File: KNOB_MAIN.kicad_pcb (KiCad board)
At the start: 2 copper layers, 100 x 30 mm, 21 parts, among them J1 HRO_TYPE-C-31-M-12, SW1 PEC11R-4220F-S0024, U1 AMS1117-3.3, U2 ESP32-C3-MINI-1

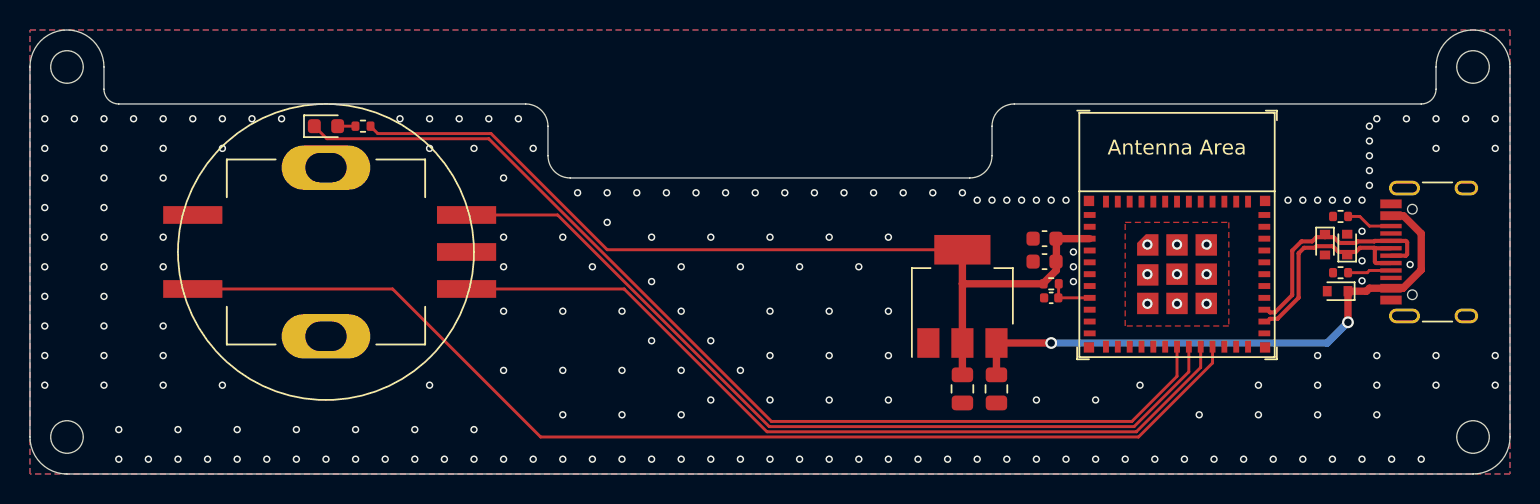
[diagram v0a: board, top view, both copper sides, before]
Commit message: Change to M3 screws
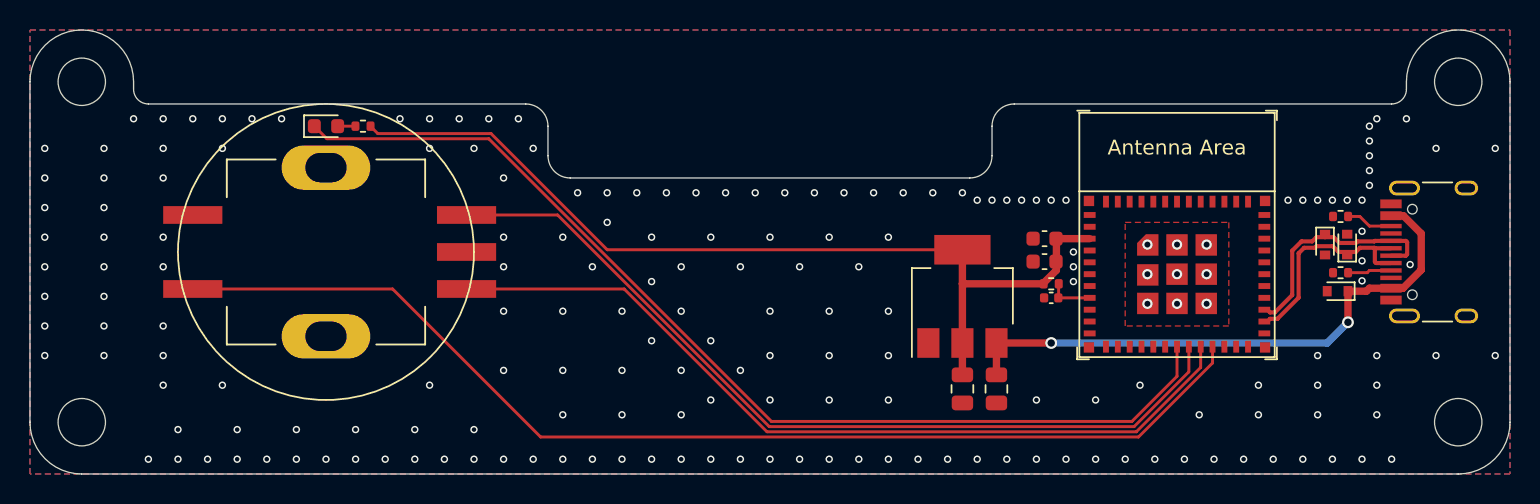
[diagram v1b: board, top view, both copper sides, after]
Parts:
- H1, H2, H3, H4: footprint MountingHole:MountingHole_2.2mm_M2 -> MountingHole:MountingHole_3.2mm_M3
- moved H1 1.41 mm to (103.5, 73.5)
- moved H2 1.41 mm to (103.5, 96.5)
- moved H3 1.41 mm to (196.5, 73.5)
- moved H4 1.41 mm to (196.5, 96.5)
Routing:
- net GND: vias 208 -> 195
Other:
- outline, holes or cut-outs redrawn
